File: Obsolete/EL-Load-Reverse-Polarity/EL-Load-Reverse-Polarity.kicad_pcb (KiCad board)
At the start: 2 copper layers, 49 x 49 mm, 49 parts, among them J1 Conn_01x02_Socket, J2 Conn_01x02_Socket, J3 Conn_01x10_Male, Q1 AOSP66923, Q2 IRFP250M, U1 MCP6V51, U5 MCP6V51

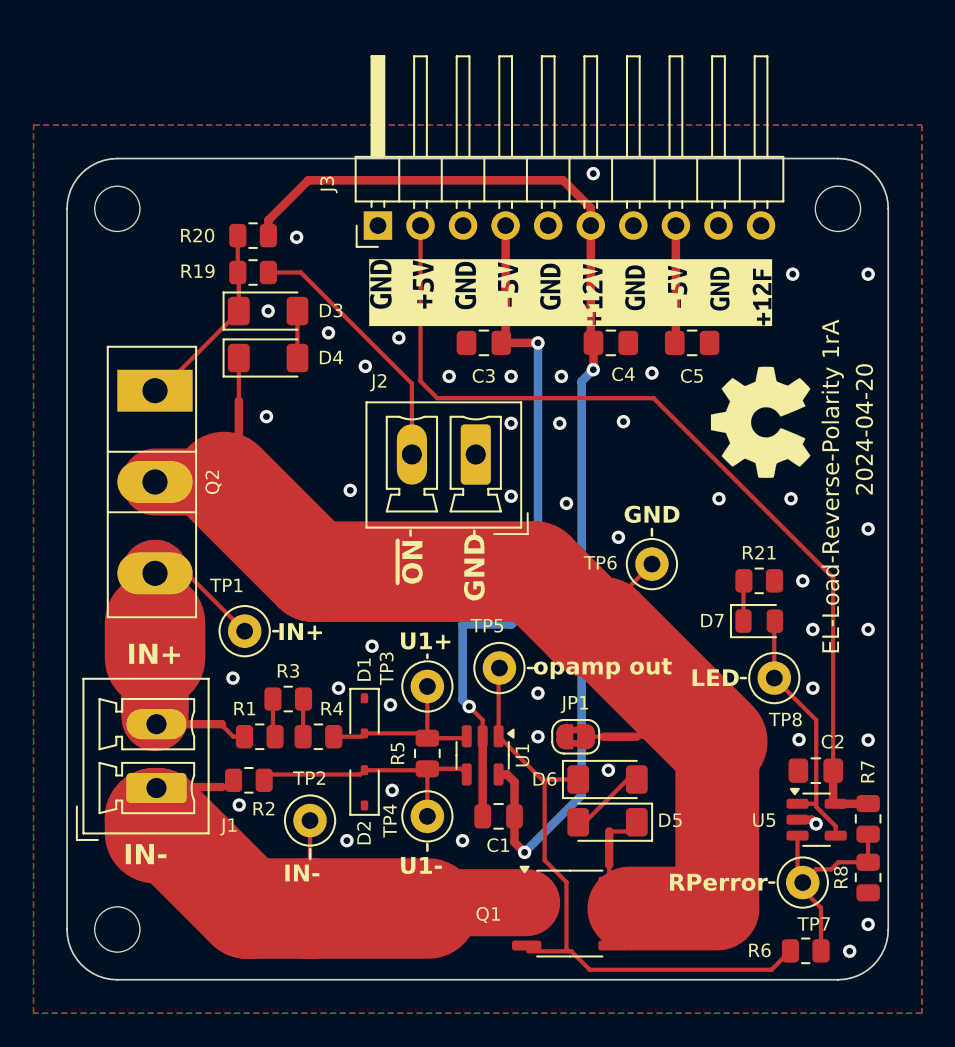
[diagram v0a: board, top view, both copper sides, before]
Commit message: New reverse polarity test schema & PCB.
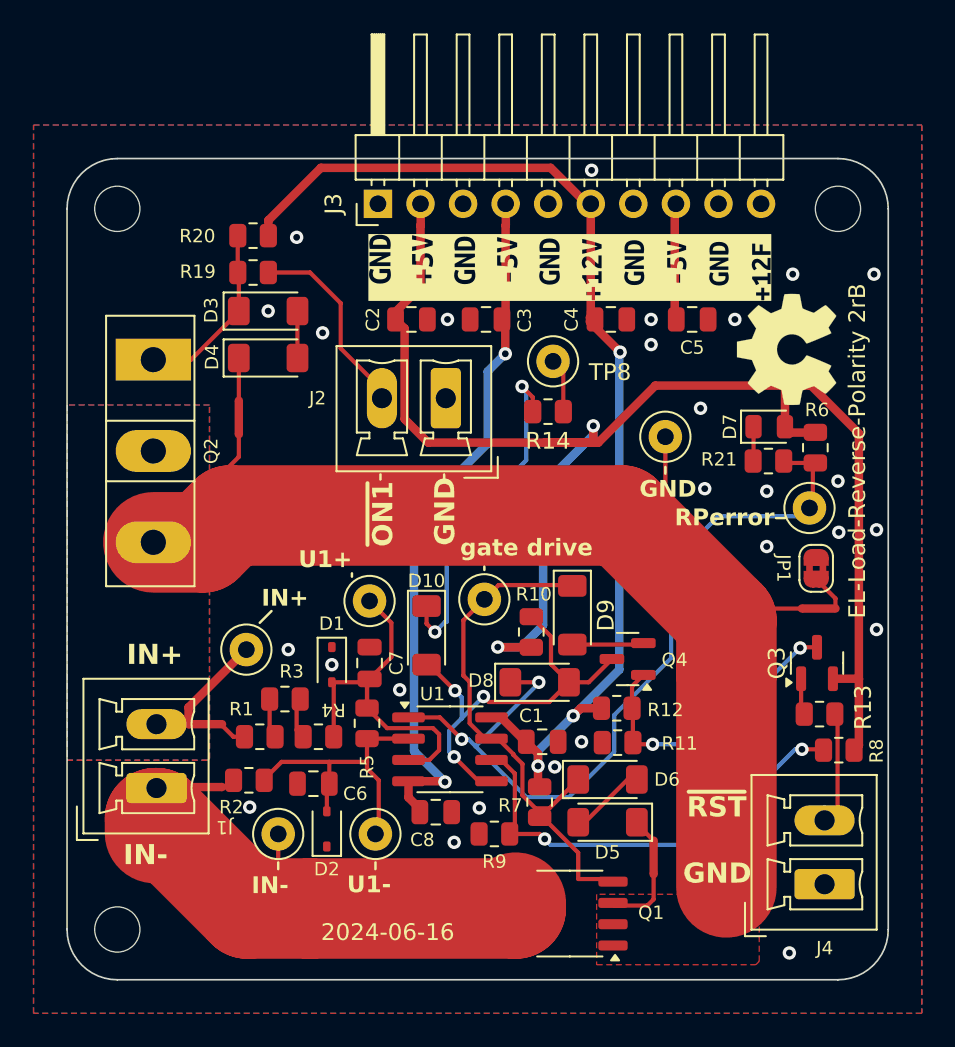
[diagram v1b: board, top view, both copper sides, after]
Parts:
- removed U5: MCP6V51, Package_TO_SOT_SMD:SOT-23-5
- added C6: 100n, Capacitor_SMD:C_0805_2012Metric, F.Cu at (90.8, 77.9)
- added C7: 100n, Capacitor_SMD:C_0805_2012Metric, F.Cu at (94.2, 70.7)
- added C8: 100n, Capacitor_SMD:C_0805_2012Metric, F.Cu at (98.1, 79.6)
- added D10: LL4148, Diode_SMD:D_MiniMELF, F.Cu at (97.5, 69.0)
- added D8: LL4148, Diode_SMD:D_MiniMELF, F.Cu at (104.3, 71.8)
- added D9: LL4148, Diode_SMD:D_MiniMELF, F.Cu at (106.2, 67.8)
- added J4: Conn_01x02_Socket, Connector_Phoenix_MC:PhoenixContact_MCV_1,5_2-G-3.81_1x02_P3.81mm_Vertical, F.Cu at (121.3, 83.9)
- added Q3: MMBT3906, Package_TO_SOT_SMD:SOT-23, F.Cu at (120.8, 70.7)
- added Q4: 2N7002, Package_TO_SOT_SMD:SOT-23, F.Cu at (109.5, 70.5)
- added R10: 100k, Resistor_SMD:R_0805_2012Metric, F.Cu at (103.8, 68.8)
- added R11: 10k, Resistor_SMD:R_0805_2012Metric, F.Cu at (109.0, 75.5)
- added R12: 180k, Resistor_SMD:R_0805_2012Metric, F.Cu at (108.9, 73.4)
- added R13: 10k, Resistor_SMD:R_0805_2012Metric, F.Cu at (121.0, 73.8)
- added R14: 10k, Resistor_SMD:R_0805_2012Metric, F.Cu at (104.8, 55.7)
- added R9: 10k, Resistor_SMD:R_0805_2012Metric, F.Cu at (101.6, 80.9)
- C2, C3, C4, C5: footprint Capacitor_SMD:C_0805_2012Metric_Pad1.18x1.45mm_HandSolder -> Capacitor_SMD:C_0805_2012Metric
- R21: value 4k7 -> 2k2
- R6: value 22k -> 10k
- R7: value 20k -> 10k
- R8: value 15k -> 10k
- SYM1: value EL-Load-Reverse-Polarity 1rA -> EL-Load-Reverse-Polarity 2rB
- U1: value MCP6V51 -> LM393; footprint Package_TO_SOT_SMD:SOT-23-5 -> Package_SO:SOIC-8_3.9x4.9mm_P1.27mm
- moved C2 36.2 mm to (96.7, 50.2), turned to 0 degrees
- moved R6 30.0 mm to (120.8, 57.9), turned to -90 degrees
- moved TP8 23.1 mm to (105.1, 52.7)
- moved TP7 22.4 mm to (120.4, 61.5)
- moved R7 19.6 mm to (104.3, 79.0)
- moved JP1 17.5 mm to (120.8, 65.0), turned to 90 degrees
- moved NT5 14.1 mm to (121.0, 67.5), turned to 180 degrees
- moved D7 11.6 mm to (118.0, 56.6)
- moved R8 7.80 mm to (122.2, 75.9), turned to 180 degrees
- moved TP6 7.64 mm to (111.8, 57.2)
- moved R21 7.17 mm to (118.0, 58.6)
- moved TP3 6.16 mm to (94.2, 67.0)
- moved C1 5.15 mm to (104.5, 75.4), turned to 180 degrees
- moved SYM1 4.62 mm to (119.0, 52.0)
- moved TP5 4.20 mm to (101.0, 66.9)
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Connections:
- C1 pad 1: -5V -> GND
- D7 pad 2: Net-(D7-A) -> +5V
- NT3 pad 2: Net-(Q2-D) -> Net-(Q2-S)
- NT4 pad 1: Net-(Q2-D) -> Net-(Q2-S)
- NT5 pad 2: Net-(Q2-D) -> Net-(Q2-S)
- Q1 pad 1: Net-(J1-Pin_1) -> Net-(Q2-S)
- Q1 pad 2: Net-(J1-Pin_1) -> Net-(Q2-S)
- Q1 pad 3: Net-(J1-Pin_1) -> Net-(Q2-S)
- Q1 pad 5: Net-(Q2-D) -> Net-(J1-Pin_1)
- Q1 pad 6: Net-(Q2-D) -> Net-(J1-Pin_1)
- Q1 pad 7: Net-(Q2-D) -> Net-(J1-Pin_1)
- Q1 pad 8: Net-(Q2-D) -> Net-(J1-Pin_1)
- Q2 pad 2: Net-(Q2-D) -> Net-(J1-Pin_2)
- Q2 pad 3: Net-(J1-Pin_2) -> Net-(Q2-S)
- R21 pad 2: GND -> Net-(D8-K)
- R6 pad 1: Net-(D6-K) -> +5V
- R6 pad 2: Net-(U5-+) -> Net-(D8-K)
- R7 pad 1: Net-(U5-+) -> Net-(D6-K)
- R7 pad 2: +5V -> +12V
- R8 pad 1: GND -> +5V
- R8 pad 2: Net-(U5-+) -> Net-(U1B--)
- TP6 pad 1: Net-(Q2-D) -> Net-(Q2-S)
- TP7 pad 1: Net-(U5-+) -> Net-(D8-K)
- TP8 pad 1: Net-(D7-A) -> Net-(R14-Pad2)
- U1 pad 1: Net-(D6-K) -> Net-(D8-K)
- U1 pad 2: -5V -> Net-(D2-A2)
- U1 pad 4: Net-(D2-A2) -> -5V
- U1 pad 5: +12V -> Net-(D10-A)
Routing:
- net Net-(Q2-S): track 0.00 -> 88.5 mm
- net Net-(Q2-D): track 67.2 -> 0.00 mm
- net Net-(D8-K): track 0.00 -> 49.5 mm, vias 0 -> 2
- net +5V: track 54.3 -> 90.9 mm, vias 0 -> 2
- net Net-(U1B--): track 0.00 -> 26.8 mm, vias 0 -> 2
- net Net-(D10-A): track 0.00 -> 25.3 mm, vias 0 -> 3
- net Net-(D10-K): track 0.00 -> 20.6 mm, vias 0 -> 2
- net Net-(Q3-C): track 0.00 -> 17.8 mm, vias 0 -> 2
- net Net-(J1-Pin_2): track 23.5 -> 5.88 mm
- net Net-(D7-A): track 15.5 -> 0.00 mm
- net Net-(U5-+): track 12.6 -> 0.00 mm
- net Net-(D1-A2): track 11.3 -> 22.4 mm
- net Net-(J4-Pin_2): track 0.00 -> 7.54 mm
- net Net-(D6-K): track 37.2 -> 31.0 mm
- net Net-(D9-A): track 0.00 -> 4.27 mm
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- added copper zone on B.Cu, net Net-(J1-Pin_2)
- added copper zone on F.Cu, net Net-(J1-Pin_2)
- added copper zone on F.Cu, net Net-(Q2-S)
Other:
- board text added: "gate drive"
- board text added: "~{ON1}"
- board text added: "~{RST}"
- board text removed: "LED"
- board text removed: "opamp out"
- board text removed: "~{ON}"
